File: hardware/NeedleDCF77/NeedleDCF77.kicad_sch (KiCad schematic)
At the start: 87 parts, among them J1 USB_C_Receptacle_USB2.0, J2 Battery, J3 DSW, J4 UART, J5 Hours, J6 Minutes, J7 Seconds, Q1 AO3401A, Q2 AO3400A, SW1 ShowDate, U1 LTC3558, U2 STM32L051C8Tx, U3 MAS6180_77kHz, U4 LT1617, U5 PT6312, U6 LM4871, Y1 8MHz, Y2 32.768kHz

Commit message: Bulk work - working on layout
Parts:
- J1: Alie (none) -> TYPE-C-31-M-12; Kelco #20110 -> (none)
- R20: value R_Small -> 22k; Kelco (none) -> #11079
- R21, R22: value R_Small -> 51k; footprint Resistor_SMD:R_0805_2012Metric_Pad1.20x1.40mm_HandSolder -> Resistor_SMD:R_0603_1608Metric_Pad0.98x0.95mm_HandSolder; Kelco (none) -> #17150
- RV1: value Hour_pot -> 10k; Kelco #6738 -> #6730
- RV2: value Minutes_pot -> 10k; Kelco (none) -> #6730
- RV3: value Second_pot -> 10k; Kelco (none) -> #6730
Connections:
- net LTC_EN2: now also U2.32 (PA11)
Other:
- note added: "91C4 - 50uA - 4k"
- note added: "Set to 5.67k"
- note added: "Set to 5k"
- note added: "Set to 6.18k"
- note added: "Simpson - 100uA - 1.82k"
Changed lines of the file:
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@@
     (stroke (width 0) (type default))
   )
+  (wire (pts (xy 299.72 95.25) (xy 303.53 95.25))
+    (stroke (width 0) (type default))
+  )
   (wire (pts (xy 205.74 43.18) (xy 205.74 44.45))
     (stroke (width 0) (type default))
@@
     (stroke (width 0) (type default))
   )
-  (text "85C1 50uA Resistance ~ 3.33kOma" (at 158.75 135.89 0)
+  (text "91C4 - 50uA - 4k" (at 229.87 134.62 0)
+    (effects (font (size 1.27 1.27)) (justify left bottom))
+  )
+  (text "Set to 5.67k" (at 196.85 149.86 0)
+    (effects (font (size 1.27 1.27)) (justify left bottom))
+  )
+  (text "Set to 5k" (at 226.06 149.86 0)
+    (effects (font (size 1.27 1.27)) (justify left bottom))
+  )
+  (text "Set to 6.18k" (at 168.91 149.86 0)
+    (effects (font (size 1.27 1.27)) (justify left bottom))
+  )
+  (text "Simpson - 100uA - 1.82k" (at 161.29 134.62 0)
+    (effects (font (size 1.27 1.27)) (justify left bottom))
+  )
+  (text "85C1 50uA Resistance ~ 3.33kOma" (at 191.77 134.62 0)
     (effects (font (size 1.27 1.27)) (justify left bottom))
   )
@@
     )
   )
+  (global_label "LTC_EN2" (shape output) (at 303.53 95.25 0) (fields_autoplaced)
+    (effects (font (size 1.27 1.27)) (justify left))
+    (property "Intersheetrefs" "${INTERSHEET_REFS}" (at 314.4375 95.25 0)
+      (effects (font (size 1.27 1.27)) (justify left) hide)
+    )
+  )
   (global_label "SWDIO" (shape output) (at 311.15 132.08 180) (fields_autoplaced)
     (effects (font (size 1.27 1.27)) (justify right))
@@
       (effects (font (size 1.27 1.27)) hide)
     )
-    (property "Kelco" "#20110" (at 38.1 41.91 0)
+    (property "Alie" "TYPE-C-31-M-12" (at 38.1 41.91 0)
       (effects (font (size 1.27 1.27)) hide)
     )
@@
       (effects (font (size 1.27 1.27)) (justify right))
     )
-    (property "Value" "Second_pot" (at 238.76 149.8599 0)
+    (property "Value" "10k" (at 238.76 149.8599 0)
       (effects (font (size 1.27 1.27)) (justify right))
     )
@@
       (effects (font (size 1.27 1.27)) hide)
     )
+    (property "Kelco" "#6730" (at 241.3 148.59 0)
+      (effects (font (size 1.27 1.27)) hide)
+    )
     (pin "1")
     (pin "2")
@@
       (effects (font (size 1.27 1.27)) (justify left))
     )
-    (property "Value" "R_Small" (at 190.5 142.2399 0)
+    (property "Value" "22k" (at 190.5 142.2399 0)
       (effects (font (size 1.27 1.27)) (justify left))
     )
@@
       (effects (font (size 1.27 1.27)) hide)
     )
+    (property "Kelco" "#11079" (at 187.96 140.97 0)
+      (effects (font (size 1.27 1.27)) hide)
+    )
     (pin "1")
     (pin "2")
@@
       (effects (font (size 1.27 1.27)) (justify left))
     )
-    (property "Value" "R_Small" (at 243.84 142.2399 0)
+    (property "Value" "51k" (at 243.84 142.2399 0)
       (effects (font (size 1.27 1.27)) (justify left))
     )
-    (property "Footprint" "Resistor_SMD:R_0805_2012Metric_Pad1.20x1.40mm_HandSolder" (at 241.3 140.97 0)
+    (property "Footprint" "Resistor_SMD:R_0603_1608Metric_Pad0.98x0.95mm_HandSolder" (at 241.3 140.97 0)
       (effects (font (size 1.27 1.27)) hide)
     )
@@
       (effects (font (size 1.27 1.27)) hide)
     )
+    (property "Kelco" "#17150" (at 241.3 140.97 0)
+      (effects (font (size 1.27 1.27)) hide)
+    )
     (pin "1")
     (pin "2")
@@
       (effects (font (size 1.27 1.27)) (justify right))
     )
-    (property "Value" "Hour_pot" (at 185.42 149.8599 0)
+    (property "Value" "10k" (at 185.42 149.8599 0)
       (effects (font (size 1.27 1.27)) (justify right))
     )
@@
       (effects (font (size 1.27 1.27)) hide)
     )
-    (property "Kelco" " #6738" (at 187.96 148.59 0)
+    (property "Kelco" "#6730" (at 187.96 148.59 0)
       (effects (font (size 1.27 1.27)) hide)
     )
@@
       (effects (font (size 1.27 1.27)) (justify right))
     )
-    (property "Value" "Minutes_pot" (at 213.36 149.8599 0)
+    (property "Value" "10k" (at 213.36 149.8599 0)
       (effects (font (size 1.27 1.27)) (justify right))
     )
@@
       (effects (font (size 1.27 1.27)) hide)
     )
+    (property "Kelco" "#6730" (at 215.9 148.59 0)
+      (effects (font (size 1.27 1.27)) hide)
+    )
     (pin "1")
     (pin "2")
@@
       (effects (font (size 1.27 1.27)) (justify left))
     )
-    (property "Value" "R_Small" (at 218.44 142.2399 0)
+    (property "Value" "51k" (at 218.44 142.2399 0)
       (effects (font (size 1.27 1.27)) (justify left))
     )
-    (property "Footprint" "Resistor_SMD:R_0805_2012Metric_Pad1.20x1.40mm_HandSolder" (at 215.9 140.97 0)
+    (property "Footprint" "Resistor_SMD:R_0603_1608Metric_Pad0.98x0.95mm_HandSolder" (at 215.9 140.97 0)
       (effects (font (size 1.27 1.27)) hide)
     )
@@
       (effects (font (size 1.27 1.27)) hide)
     )
+    (property "Kelco" "#17150" (at 215.9 140.97 0)
+      (effects (font (size 1.27 1.27)) hide)
+    )

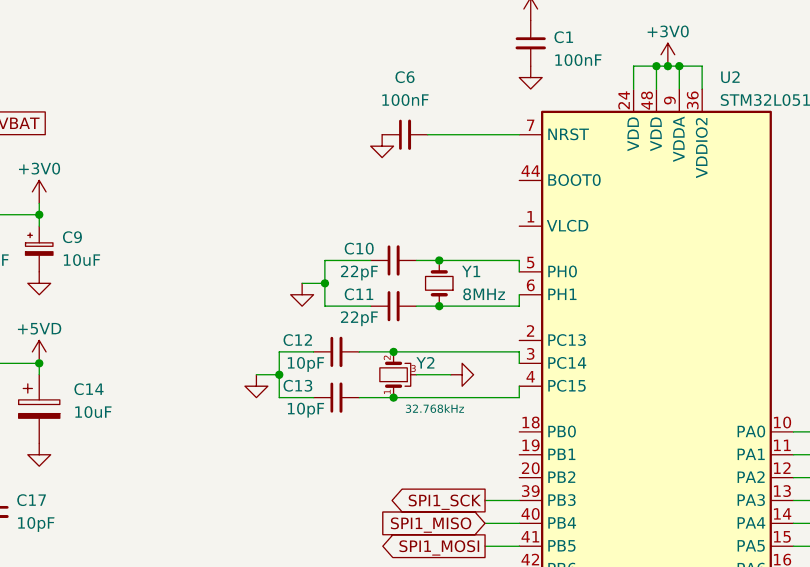
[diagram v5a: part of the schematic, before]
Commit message: Use HSI instead of HSE
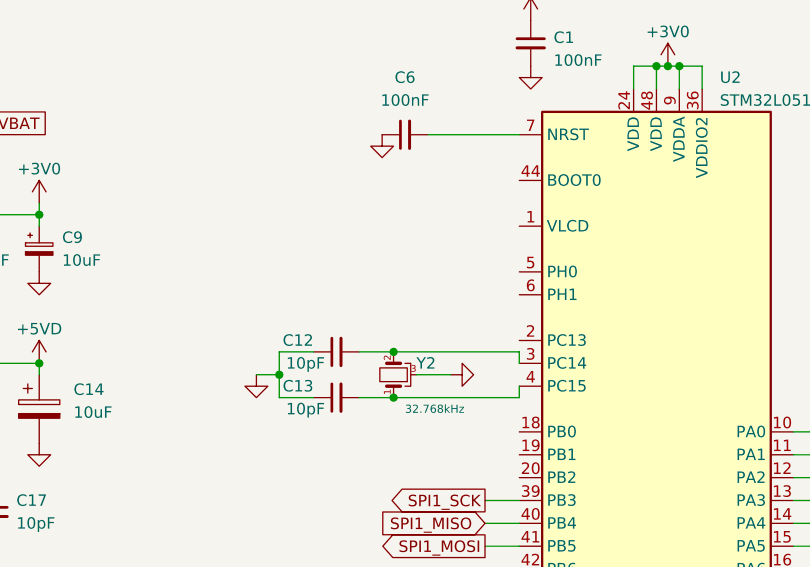
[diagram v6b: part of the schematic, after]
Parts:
- removed C10, C11: 22pF, Capacitor_SMD:C_0805_2012Metric_Pad1.18x1.45mm_HandSolder, symbol Device:C_Small
- removed Y1: 8MHz, Crystal:Crystal_SMD_HC49-SD_HandSoldering, symbol Device:Crystal_Small
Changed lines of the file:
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@@
   (junction (at 195.58 71.12) (diameter 0) (color 0 0 0 0)
   )
-  (junction (at 260.35 53.34) (diameter 0) (color 0 0 0 0)
-  )
   (junction (at 68.58 116.84) (diameter 0) (color 0 0 0 0)
   )
@@
   (junction (at 205.74 107.95) (diameter 0) (color 0 0 0 0)
   )
-  (junction (at 260.35 48.26) (diameter 0) (color 0 0 0 0)
-  )
   (junction (at 43.18 116.84) (diameter 0) (color 0 0 0 0)
   )
@@
   (junction (at 215.9 59.69) (diameter 0) (color 0 0 0 0)
   )
-  (junction (at 247.65 50.8) (diameter 0) (color 0 0 0 0)
-  )
   (junction (at 71.12 92.71) (diameter 0) (color 0 0 0 0)
   )
@@
     (stroke (width 0) (type default))
   )
-  (wire (pts (xy 247.65 48.26) (xy 252.73 48.26))
-    (stroke (width 0) (type default))
-  )
   (wire (pts (xy 137.16 139.7) (xy 143.51 139.7))
     (stroke (width 0) (type default))
@@
     (stroke (width 0) (type default))
   )
-  (wire (pts (xy 269.24 52.07) (xy 269.24 53.34))
-    (stroke (width 0) (type default))
-  )
   (wire (pts (xy 123.19 119.38) (xy 120.65 119.38))
     (stroke (width 0) (type default))
@@
     (stroke (width 0) (type default))
   )
-  (wire (pts (xy 257.81 53.34) (xy 260.35 53.34))
-    (stroke (width 0) (type default))
-  )
   (wire (pts (xy 147.32 68.58) (xy 147.32 74.93))
     (stroke (width 0) (type default))
@@
     (stroke (width 0) (type default))
   )
-  (wire (pts (xy 245.11 50.8) (xy 247.65 50.8))
-    (stroke (width 0) (type default))
-  )
   (wire (pts (xy 215.9 151.13) (xy 215.9 153.67))
     (stroke (width 0) (type default))
@@
     (stroke (width 0) (type default))
   )
-  (wire (pts (xy 247.65 53.34) (xy 247.65 50.8))
-    (stroke (width 0) (type default))
-  )
   (wire (pts (xy 251.46 58.42) (xy 255.27 58.42))
     (stroke (width 0) (type default))
@@
     (stroke (width 0) (type default))
   )
-  (wire (pts (xy 269.24 48.26) (xy 260.35 48.26))
-    (stroke (width 0) (type default))
-  )
   (wire (pts (xy 212.09 138.43) (xy 215.9 138.43))
     (stroke (width 0) (type default))
@@
     (stroke (width 0) (type default))
   )
-  (wire (pts (xy 252.73 53.34) (xy 247.65 53.34))
-    (stroke (width 0) (type default))
-  )
   (wire (pts (xy 67.31 31.75) (xy 67.31 34.29))
     (stroke (width 0) (type default))
@@
     (stroke (width 0) (type default))
   )
-  (wire (pts (xy 257.81 48.26) (xy 260.35 48.26))
-    (stroke (width 0) (type default))
-  )
   (bus (pts (xy 107.95 113.03) (xy 110.49 113.03))
     (stroke (width 0) (type default))
@@
     (stroke (width 0) (type default))
   )
-  (wire (pts (xy 247.65 50.8) (xy 247.65 48.26))
-    (stroke (width 0) (type default))
-  )
   (bus (pts (xy 146.05 124.46) (xy 146.05 127))
     (stroke (width 0) (type default))
@@
     (stroke (width 0) (type default))
   )
-  (wire (pts (xy 269.24 49.53) (xy 269.24 48.26))
-    (stroke (width 0) (type default))
-  )
   (wire (pts (xy 255.27 63.5) (xy 269.24 63.5))
     (stroke (width 0) (type default))
@@
     (stroke (width 0) (type default))
   )
-  (wire (pts (xy 260.35 53.34) (xy 269.24 53.34))
-    (stroke (width 0) (type default))
-  )
   (wire (pts (xy 107.95 106.68) (xy 107.95 110.49))
     (stroke (width 0) (type default))
@@
     )
   )
-  (symbol (lib_id "Device:C_Small") (at 255.27 53.34 90) (unit 1)
-    (in_bom yes) (on_board yes) (dnp no)
-    (property "Reference" "C11" (at 251.46 52.07 90)
-      (effects (font (size 1.27 1.27)))
-    )
-    (property "Value" "22pF" (at 251.46 54.61 90)
-      (effects (font (size 1.27 1.27)))
-    )
-    (property "Footprint" "Capacitor_SMD:C_0805_2012Metric_Pad1.18x1.45mm_HandSolder" (at 255.27 53.34 0)
-      (effects (font (size 1.27 1.27)) hide)
-    )
-    (property "Datasheet" "~" (at 255.27 53.34 0)
-      (effects (font (size 1.27 1.27)) hide)
-    )
-    (property "Kelco" "#10038" (at 255.27 53.34 90)
-      (effects (font (size 1.27 1.27)) hide)
-    )
-    (pin "1")
-    (pin "2")
-    (instances
-      (project "NeedleDCF77"
-        (path "/9538e4ed-27e6-4c37-b989-9859dc0d49e8"
-          (reference "C11") (unit 1)
-        )
-      )
-    )
-  )
   (symbol (lib_id "Device:C_Polarized") (at 215.9 64.77 0) (unit 1)
     (in_bom yes) (on_board yes) (dnp no) (fields_autoplaced)
@@
     )
   )
-  (symbol (lib_id "Device:Crystal_Small") (at 260.35 50.8 90) (unit 1)
-    (in_bom yes) (on_board yes) (dnp no) (fields_autoplaced)
-    (property "Reference" "Y1" (at 262.89 49.5299 90)
-      (effects (font (size 1.27 1.27)) (justify right))
-    )
-    (property "Value" "8MHz" (at 262.89 52.0699 90)
-      (effects (font (size 1.27 1.27)) (justify right))
-    )
-    (property "Footprint" "Crystal:Crystal_SMD_HC49-SD_HandSoldering" (at 260.35 50.8 0)
-      (effects (font (size 1.27 1.27)) hide)
-    )
-    (property "Datasheet" "~" (at 260.35 50.8 0)
-      (effects (font (size 1.27 1.27)) hide)
-    )
-    (property "Kelco" "#19702" (at 260.35 50.8 90)
-      (effects (font (size 1.27 1.27)) hide)
-    )
-    (pin "1")
-    (pin "2")
-    (instances
-      (project "NeedleDCF77"
-        (path "/9538e4ed-27e6-4c37-b989-9859dc0d49e8"
-          (reference "Y1") (unit 1)
-        )
-      )
-    )
-  )
   (symbol (lib_id "Device:R_Small") (at 107.95 124.46 0) (unit 1)
     (in_bom yes) (on_board yes) (dnp no) (fields_autoplaced)
@@
     )
   )
-  (symbol (lib_id "power:GND") (at 245.11 50.8 0) (unit 1)
-    (in_bom yes) (on_board yes) (dnp no) (fields_autoplaced)
-    (property "Reference" "#PWR0123" (at 245.11 57.15 0)
-      (effects (font (size 1.27 1.27)) hide)
-    )
-    (property "Value" "GND" (at 247.65 52.0699 0)
-      (effects (font (size 1.27 1.27)) (justify left) hide)
-    )
-    (property "Footprint" "" (at 245.11 50.8 0)
-      (effects (font (size 1.27 1.27)) hide)
-    )
-    (property "Datasheet" "" (at 245.11 50.8 0)
-      (effects (font (size 1.27 1.27)) hide)
-    )
-    (pin "1")
-    (instances
-      (project "NeedleDCF77"
-        (path "/9538e4ed-27e6-4c37-b989-9859dc0d49e8"
-          (reference "#PWR0123") (unit 1)
-        )
-      )
-    )
-  )
   (symbol (lib_id "Device:R_Small") (at 203.2 74.93 0) (unit 1)
     (in_bom yes) (on_board yes) (dnp no)
@@
         )
       )
-    )
-  )
-  (symbol (lib_id "Device:C_Small") (at 255.27 48.26 90) (unit 1)
-    (in_bom yes) (on_board yes) (dnp no)
-    (property "Reference" "C10" (at 251.46 46.99 90)
-      (effects (font (size 1.27 1.27)))
-    )
-    (property "Value" "22pF" (at 251.46 49.53 90)
-      (effects (font (size 1.27 1.27)))
-    )
-    (property "Footprint" "Capacitor_SMD:C_0805_2012Metric_Pad1.18x1.45mm_HandSolder" (at 255.27 48.26 0)
-      (effects (font (size 1.27 1.27)) hide)
-    )
-    (property "Datasheet" "~" (at 255.27 48.26 0)
-      (effects (font (size 1.27 1.27)) hide)
-    )
-    (property "Kelco" "#10038" (at 255.27 48.26 90)
-      (effects (font (size 1.27 1.27)) hide)
-    )
-    (pin "1")
-    (pin "2")
-    (instances
-      (project "NeedleDCF77"
-        (path "/9538e4ed-27e6-4c37-b989-9859dc0d49e8"
-          (reference "C10") (unit 1)
-        )
-      )
